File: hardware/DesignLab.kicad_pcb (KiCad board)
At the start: 2 copper layers, 169.9 x 180.3 mm, 87 parts, among them J1 Micro_SD_Card_Det, J2 Conn_01x04_Female, P1 USB_C_Plug_USB2.0, Q1 DMG3415U-7, SW1 SW_DPDT_x2, SW10 Button, SW11 Button, SW12 RESET, SW13 ON, SW14 VOL, SW15 BOOT, SW2 SW_DPDT_x2, SW3 REC, SW4 Button, SW5 Button, SW6 Button, SW7 Button, SW8 Button, SW9 Button, U1 SPH0641LM4H, U10 MCP4018-xxxxLT, U2 RP2040, U3 QRE1113, U4 QRE1113, U5 QRE1113, U6 AT25SF128A, U7 PAM8302AAD, U8 AP2112K-3.3, U9 QRE1113, Y1 12Mhz

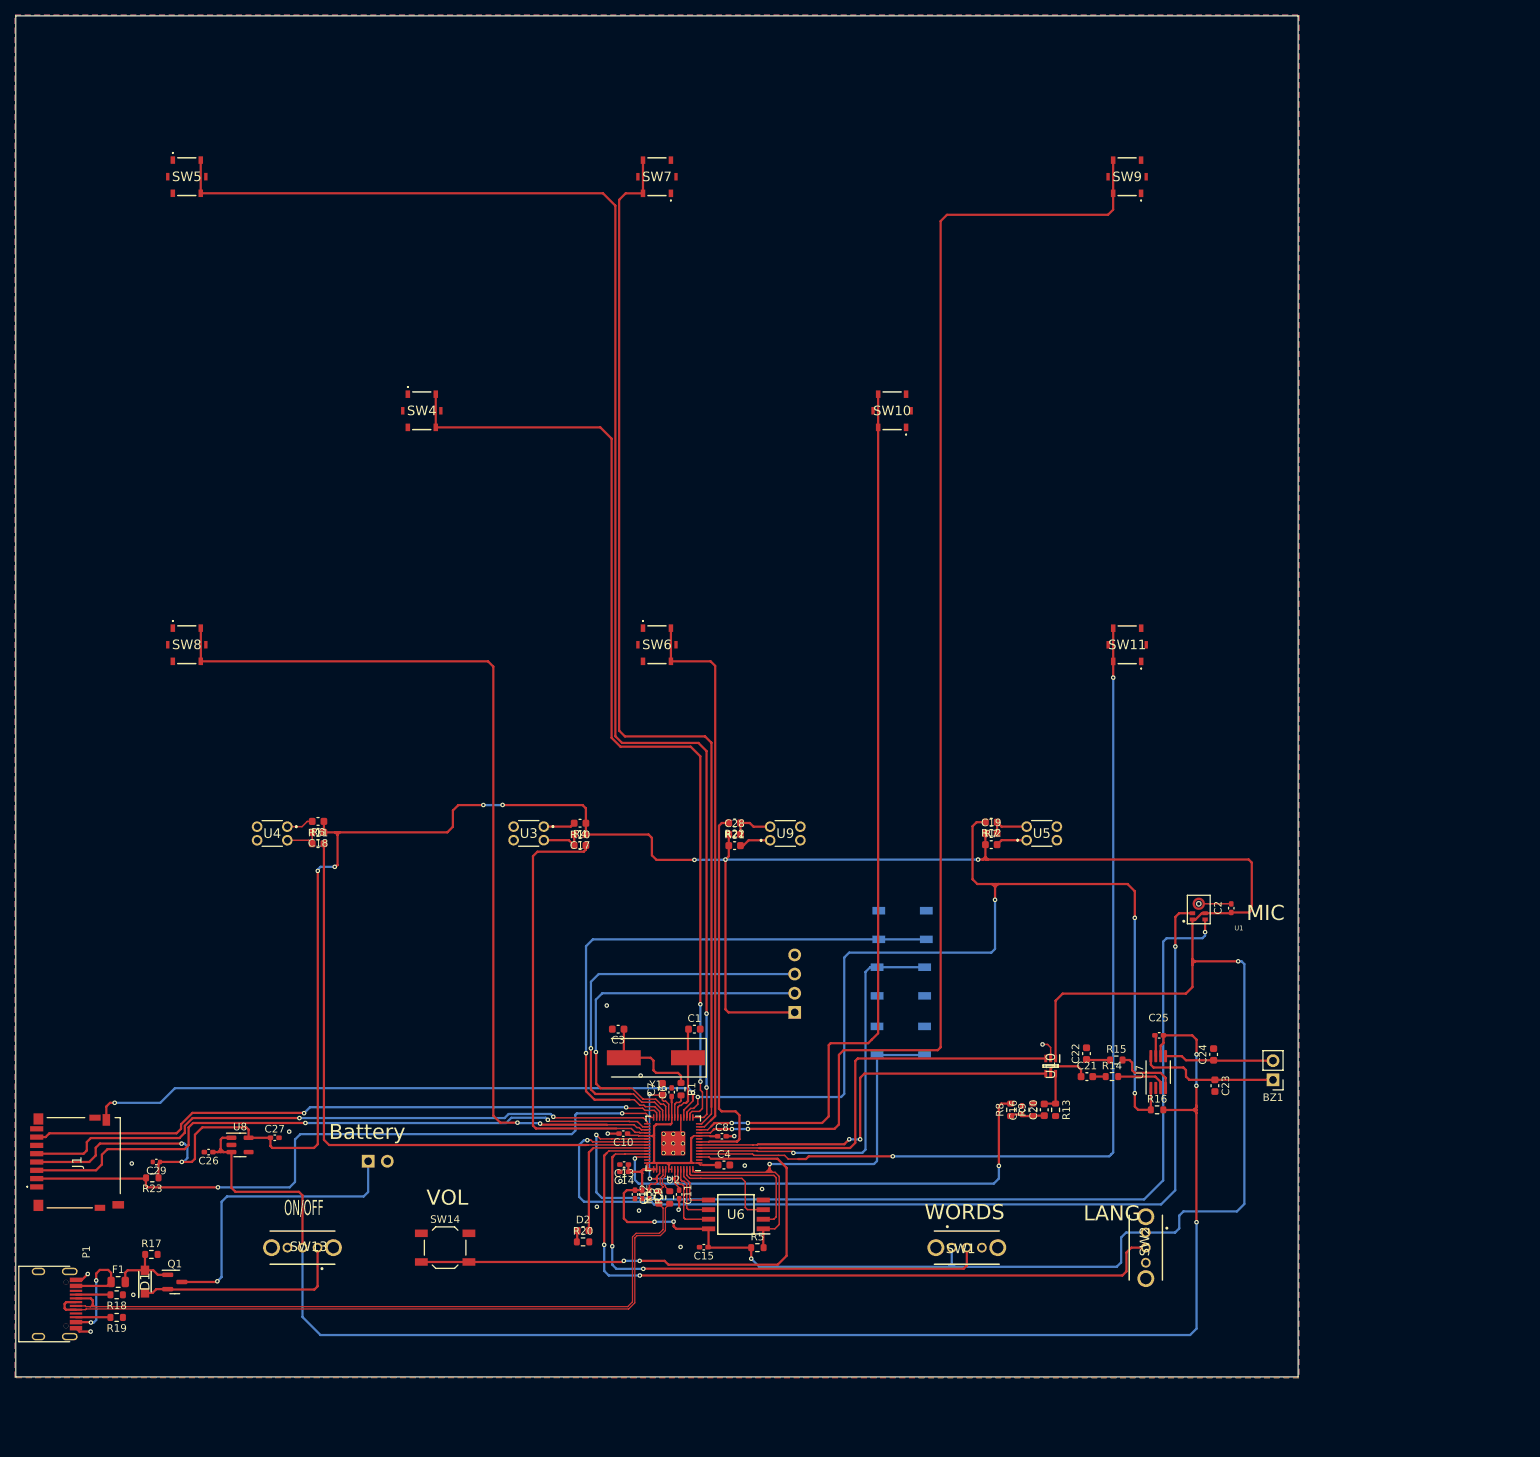
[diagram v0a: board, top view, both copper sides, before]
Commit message: Corrections to the schematic and the PCB
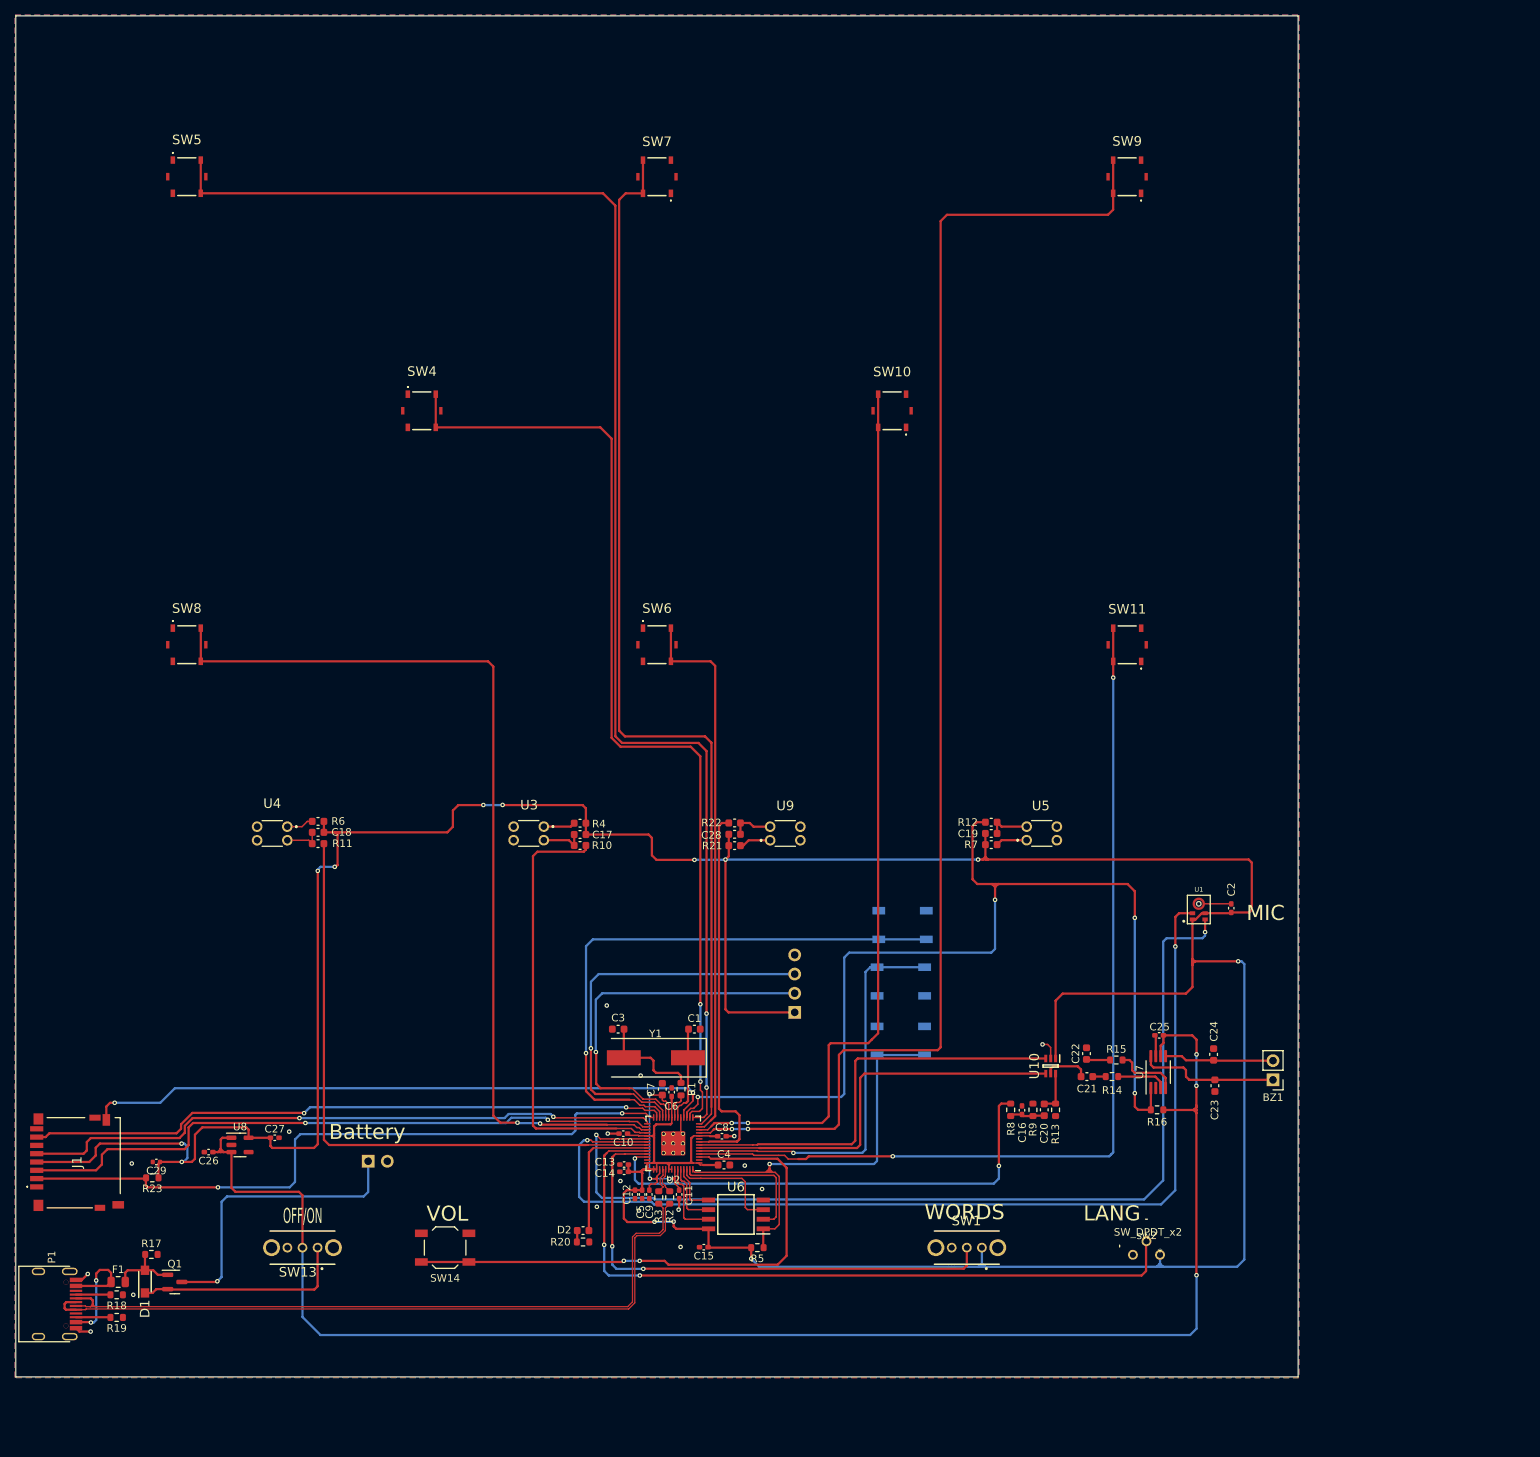
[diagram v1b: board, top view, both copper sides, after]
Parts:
- sw2: renamed from SW2; footprint Design:OS102011MA1QN1 -> Design:7829H-1-051LF
- moved sw2 2.11 mm to (270.8, 194.9), turned to 180 degrees
- turned SW1 to 180 degrees
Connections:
- U10 pad 3: /SDA -> /SCL
- U10 pad 4: /SCL -> /SDA
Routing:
- net +3V3: track 508.8 -> 513.1 mm
- net /SCL: track 54.6 -> 56.9 mm, vias 2 -> 0
- net /SDA: track 57.4 -> 55.5 mm
- net /LANG: track 96.3 -> 97.7 mm
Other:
- board text added: "BOOT"
- board text added: "OFF/ON"
- board text added: "RST"
- board text removed: "ON/OFF"

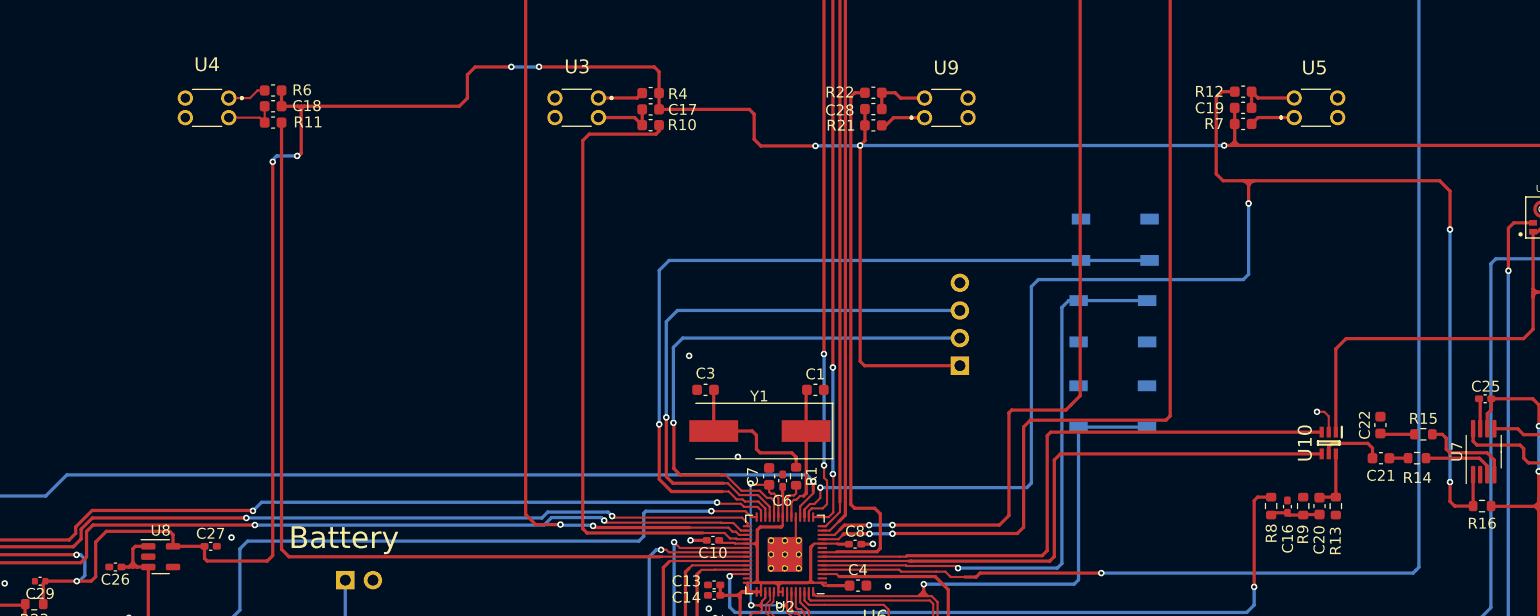
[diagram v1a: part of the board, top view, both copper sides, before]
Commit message: Sensors corrected
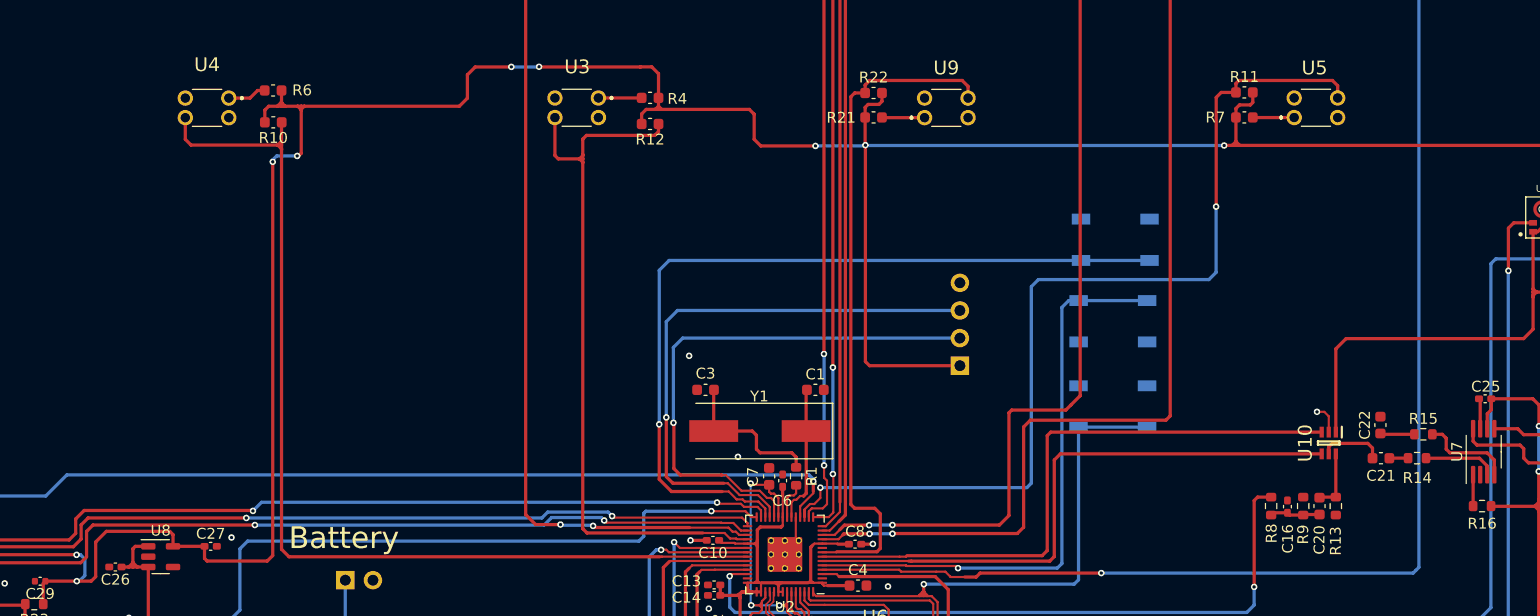
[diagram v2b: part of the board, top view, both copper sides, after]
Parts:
- removed C17, C18, C19, C28: 10nF, Capacitor_SMD:C_0603_1608Metric
- R10, R11, R12, R22: value 220 -> 10K
- U7: value PAM8302AAD -> PAM8302AASCR
- moved R11 89.4 mm to (248.5, 137.7)
- moved R12 54.6 mm to (193.8, 140.6)
- moved R10 34.7 mm to (159.2, 140.4), turned to 180 degrees
- moved R21 0.73 mm to (214.4, 139.9)
- moved R7 0.61 mm to (248.5, 139.9)
- moved R4 0.44 mm to (193.8, 138.2)
- turned R22 to 0 degrees
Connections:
- R10 pad 1: Net-(C17-Pad2) -> /S2
- R10 pad 2: /S3 -> +3V3
- R11 pad 1: Net-(C18-Pad2) -> /S1
- R11 pad 2: /S2 -> +3V3
- R12 pad 1: Net-(C19-Pad2) -> /S3
- R12 pad 2: /S1 -> +3V3
- R16 pad 1: /S1 -> Net-(R16-Pad1)
- R22 pad 1: Net-(C28-Pad2) -> /S4
- R22 pad 2: /S4 -> +3V3
- U3 pad 3: GND -> /S3
- U3 pad 4: Net-(C17-Pad2) -> GND
- U4 pad 3: GND -> /S2
- U4 pad 4: Net-(C18-Pad2) -> GND
- U5 pad 3: GND -> /S1
- U5 pad 4: Net-(C19-Pad2) -> GND
- U7 pad 1: /S1 -> Net-(R16-Pad1)
- U9 pad 3: GND -> /S4
- U9 pad 4: Net-(C28-Pad2) -> GND
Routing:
- net /S1: track 136.9 -> 89.2 mm, vias 4 -> 2
- net /S2: track 82.4 -> 94.5 mm
- net /S4: track 50.7 -> 62.3 mm
- net +3V3: track 513.1 -> 524.4 mm
- net /S3: track 59.2 -> 66.5 mm
- net Net-(C17-Pad2): track 5.76 -> 0.00 mm
- net Net-(C19-Pad2): track 5.65 -> 0.00 mm
- net Net-(C28-Pad2): track 5.64 -> 0.00 mm
- net Net-(C18-Pad2): track 4.99 -> 0.00 mm
- net Net-(R16-Pad1): track 0.00 -> 2.89 mm

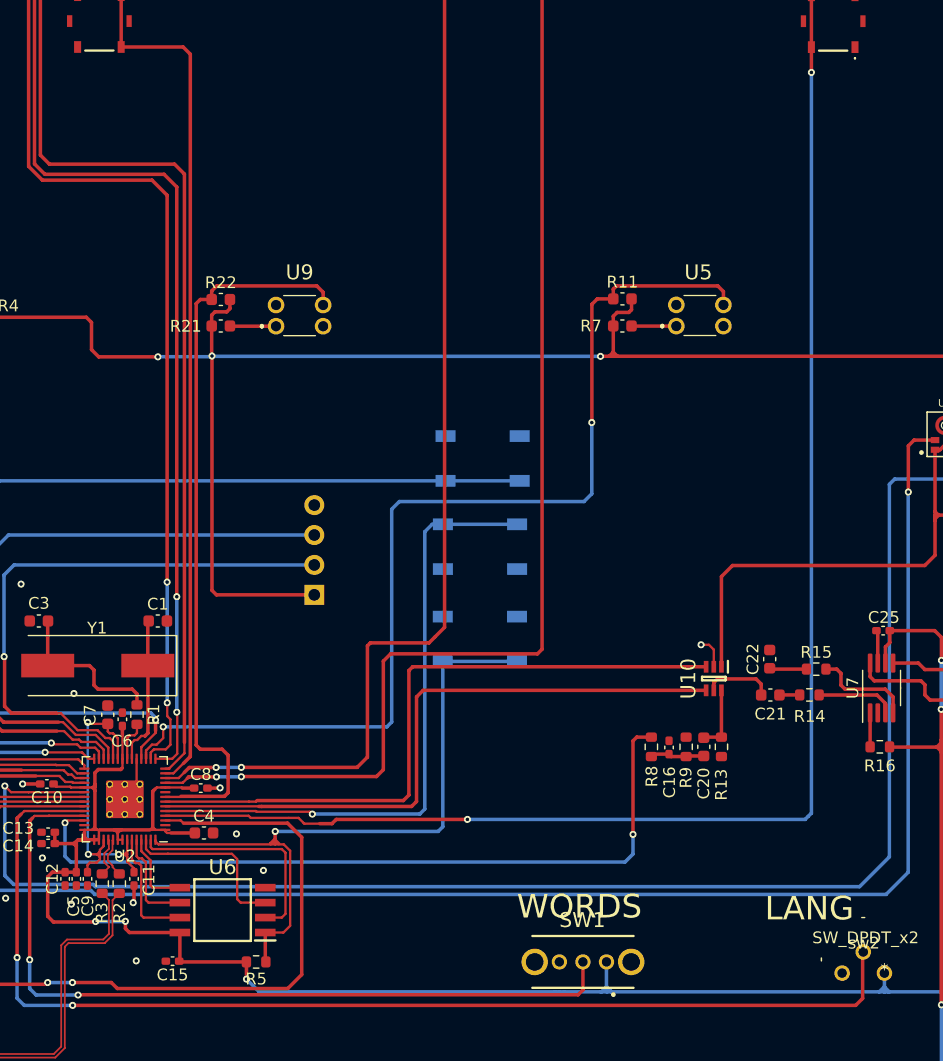
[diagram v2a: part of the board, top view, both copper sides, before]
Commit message: EN_SOUND routed
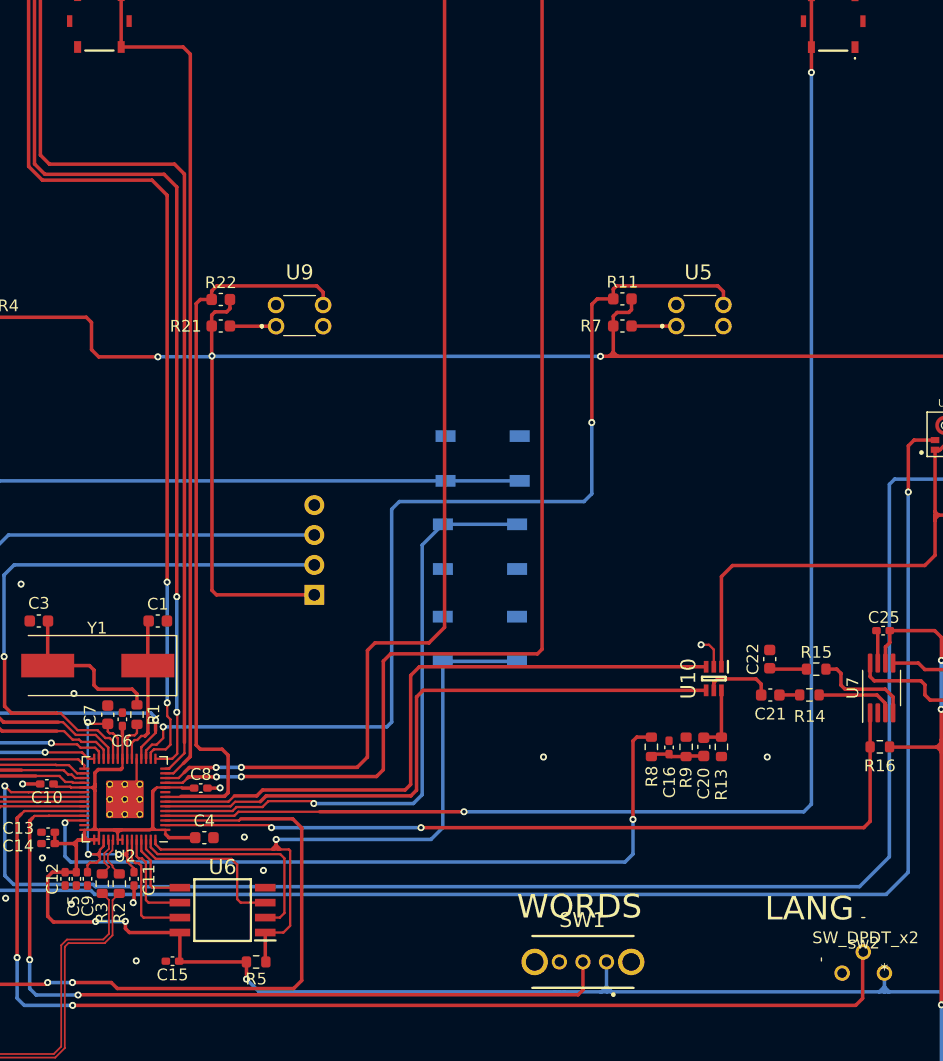
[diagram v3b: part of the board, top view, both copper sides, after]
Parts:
- U6: value AT25SF128A -> W25Q80DVSSIG
- moved C4 0.40 mm to (213.0, 183.4)
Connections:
- R16 pad 1: Net-(R16-Pad1) -> /EN_SOUND
- U7 pad 1: Net-(R16-Pad1) -> /EN_SOUND
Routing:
- net /EN_SOUND: track 0.00 -> 69.4 mm, vias 0 -> 2
- net Net-(R16-Pad1): track 2.89 -> 0.00 mm
- net /REC: track 54.0 -> 52.5 mm
- net /D4: track 125.0 -> 124.0 mm
- net /VOL: track 73.0 -> 73.9 mm
- net /SDA: track 55.5 -> 54.6 mm
- net /SCL: track 56.9 -> 56.1 mm
- net GND: vias 17 -> 19
